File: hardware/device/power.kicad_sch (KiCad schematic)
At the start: 44 parts, among them IC3 SP3401-02UTG, J1 POT_CONN, J2 USB, U20 TPS62A02DRL, U21 TPS560200, U22 MAX17261xxTD, U23 BQ21040DBV, U26 FUSB303BTMX, U27 FUSB302B01MPX, U31 FUSB302B01MPX, U32 LTC2942

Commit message: chore: schematic organization
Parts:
- removed U22: MAX17261xxTD, Package_DFN_QFN:TDFN-14-1EP_3x3mm_P0.4mm_EP1.78x2.35mm, symbol Battery_Management:MAX17261xxTD
- removed U26: FUSB303BTMX, Package_DFN_QFN:Texas_X2QFN-12_1.6x1.6mm_P0.4mm, symbol Interface_USB:FUSB303BTMX
- removed U27: FUSB302B01MPX, Package_DFN_QFN:WQFN-14-1EP_2.5x2.5mm_P0.5mm_EP1.45x1.45mm, symbol Interface_USB:FUSB302B01MPX
- added C19, C20: 1uF, symbol Device:C
- added R38: 675R, Resistor_SMD:R_0402_1005Metric, symbol Device:R
- added U22: BQ24072RGT, Package_DFN_QFN:VQFN-16-1EP_3x3mm_P0.5mm_EP1.6x1.6mm, symbol Battery_Management:BQ24072RGT
- added U26: BQ25040, Package_SON:WSON-10-1EP_2x3mm_P0.5mm_EP0.84x2.4mm_ThermalVias, symbol Battery_Management:BQ25040
- C11, C12, C13, C14, C15, C16, C17, C18, C9, R12, R2, R20, R21, R23, R24, R26, R27, R29, R33: footprint (none) -> Capacitor_SMD:C_0402_1005Metric
- IC3: JLC (none) -> C3702190
- J1: JLC (none) -> C5527934
- J2: JLC (none) -> C2988369
- R34: footprint (none) -> Resistor_SMD:R_0402_1005Metric
- R63, R72: footprint Resistor_SMD:R_0603_1608Metric_Pad0.98x0.95mm_HandSolder -> Capacitor_SMD:C_0402_1005Metric
- U31: JLC (none) -> C488155
- U32: JLC (none) -> C683656
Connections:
- net +3.3V: now also R34.1
- net GND: now also U23.5 (GND), C19.2, C20.2
- net +BATT: now reaches R33.1, U32.1 (SENSE+)
- net +BATT: now also U23.2 (OUT), C20.1
- net at U23.6 (VIN): now also C19.1
- new net: U22.10 (OUT), U22.11 (OUT)
- new net: U22.17 (VSS), U22.8 (VSS)
- new net: U22.2 (BAT), U22.3 (BAT)
- new net: U26.11 (VSS), U26.3 (VSS), U26.7 (VSS)
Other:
- note added: "Charging and draw for battery MUST pass through the fuel gauge current-sense resistor to properly detect discharging."
- note added: "DRP (Dual-Role-Port)"
- note added: "FUSB302B has a "dead battery" feature, enabling Rd resistors on CC lines when the FUSB302B is not powered to allow it to attach as a sink device even when it is not powered."
- note added: "See FUSB302 CONTROL2 register for dual-model device via the autonomous DRP toggle."
- note added: "TODO: checl ISET resistor"
- note added: "Used by the STM32 to detect when a USB cable has been plugged in or removed. Expected signal < 4v"
- note added: "https://www.usb.org/document-library/usb-power-delivery"
- note removed: "BQ24070RHLR?"
- moved on the sheet: BT1, C17, C18, IC3, J2, R29, R33, R34, U23, U31, U32

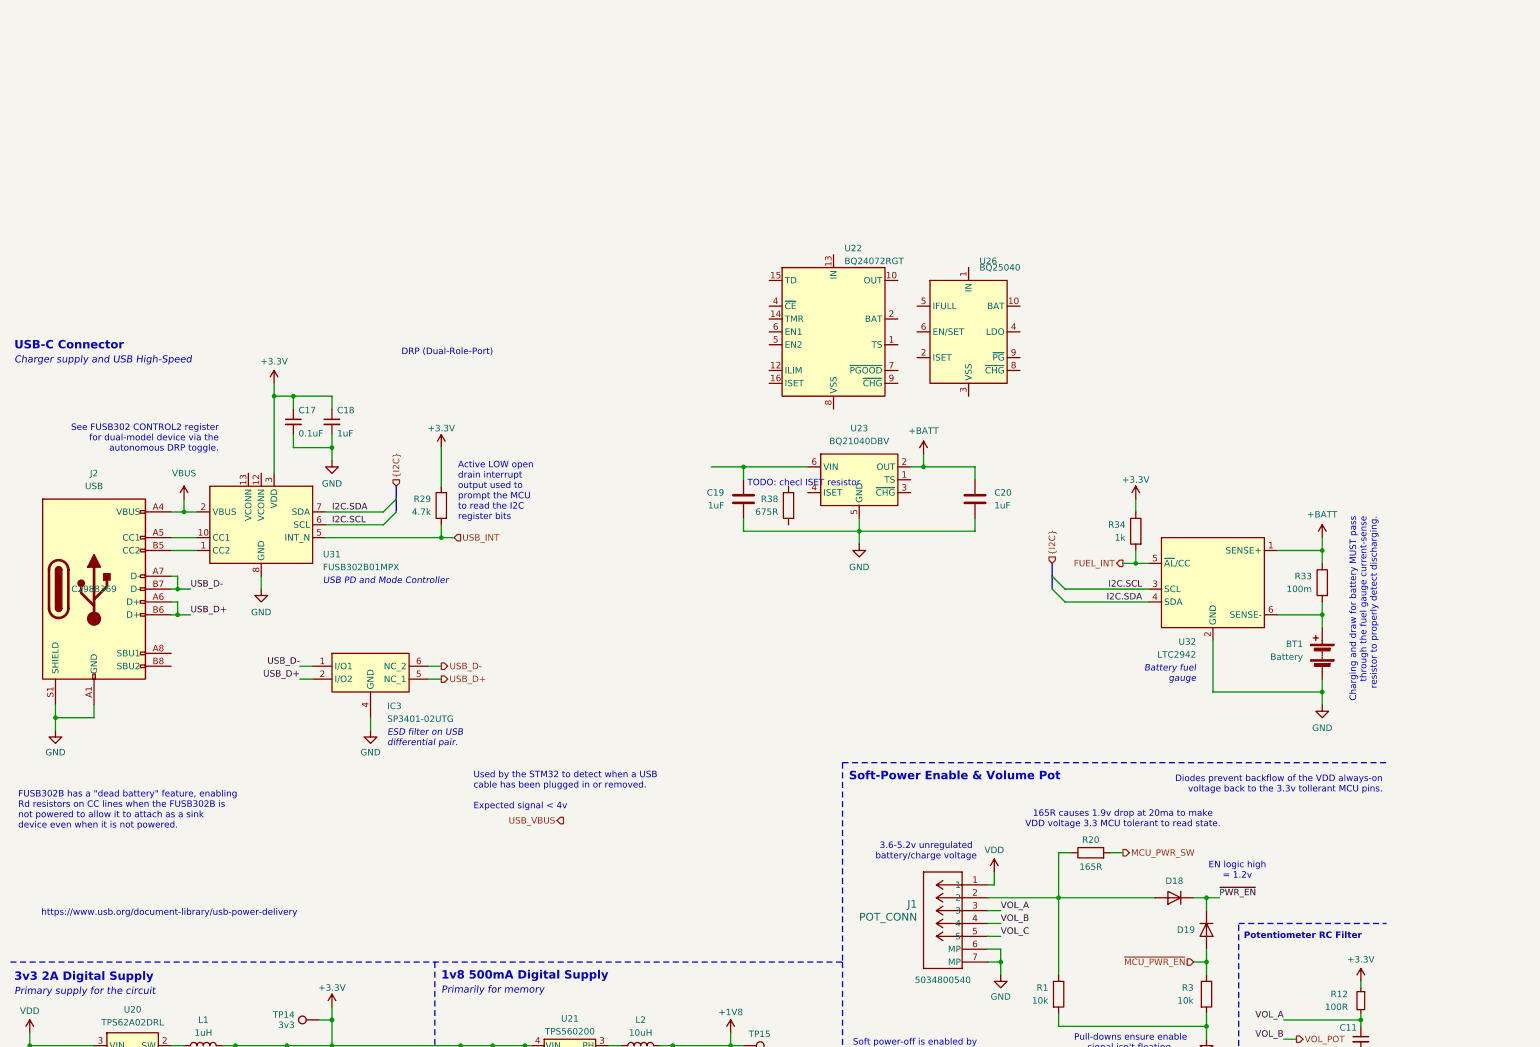
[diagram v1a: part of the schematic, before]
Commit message: feat: add plated mounting holes
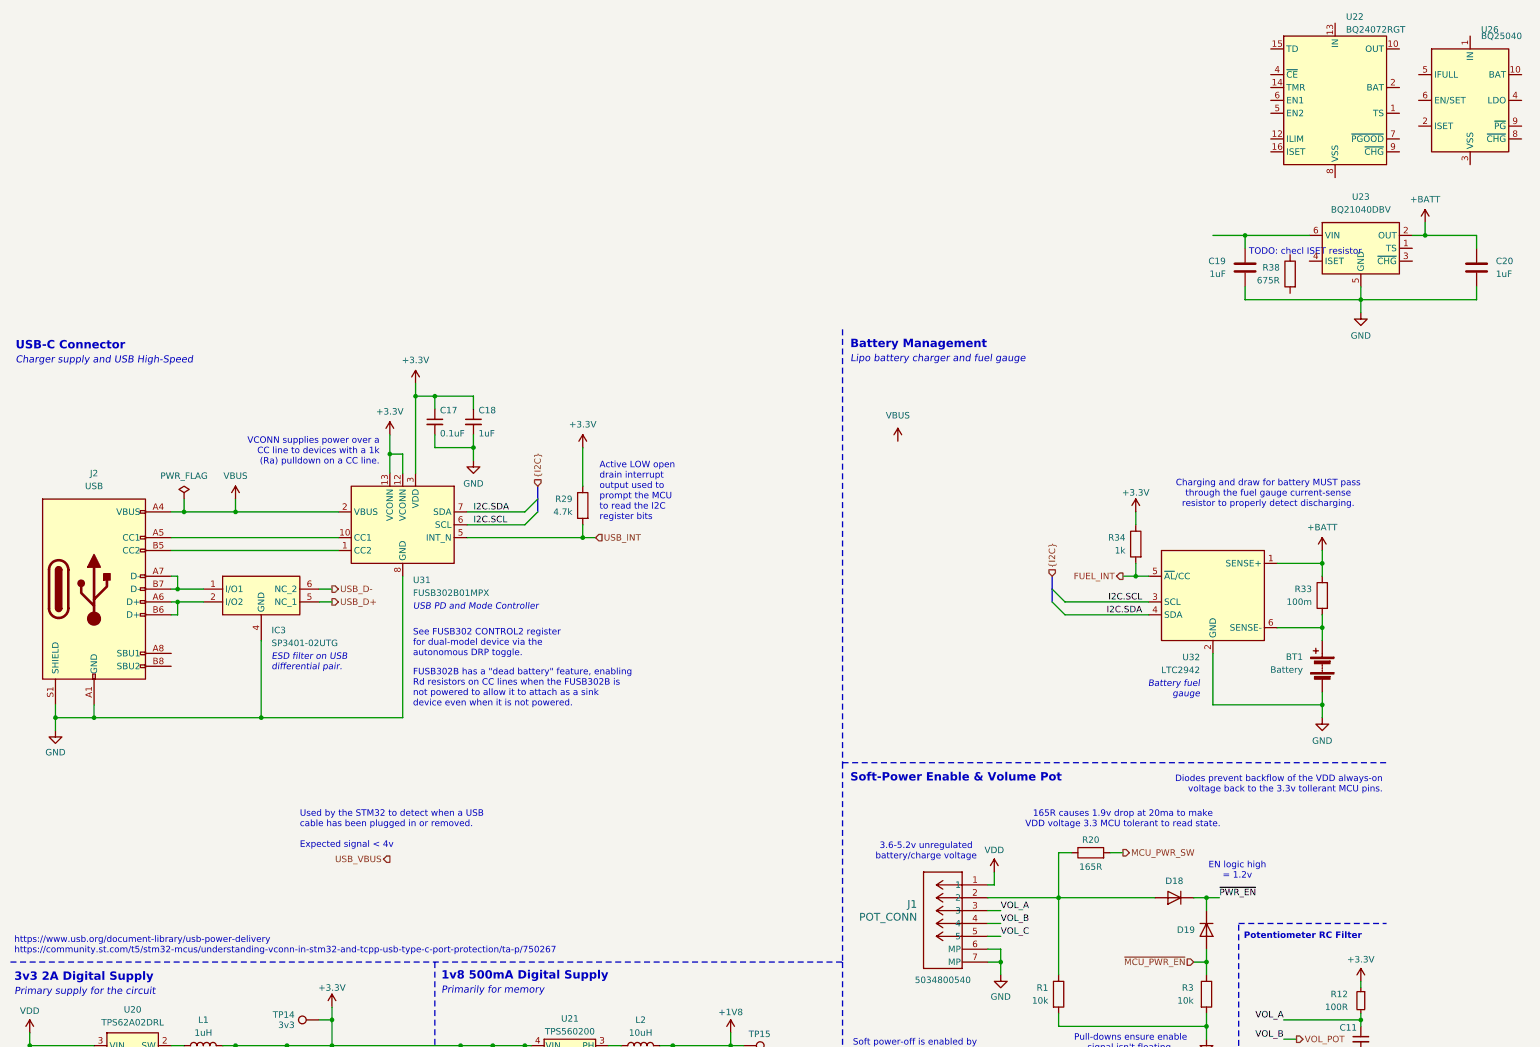
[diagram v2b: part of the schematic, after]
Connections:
- net +3.3V: now also U31.12 (VCONN), U31.13 (VCONN)
- net USB_D+: no longer IC3.2 (I/O2), J2.A6 (D+), J2.B6 (D+)
- net USB_D-: no longer IC3.1 (I/O1), J2.A7 (D-), J2.B7 (D-)
- new net: IC3.2 (I/O2), J2.A6 (D+), J2.B6 (D+)
- new net: IC3.1 (I/O1), J2.A7 (D-), J2.B7 (D-)
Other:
- note added: "Battery Management"
- note added: "Lipo battery charger and fuel gauge"
- note added: "VCONN supplies power over a CC line to devices with a 1k (Ra) pulldown on a CC line."
- note added: "https://www.usb.org/document-library/usb-power-delivery https://community.st.com/t5/stm32-mcus/understanding-vconn-in-stm32-and-tcpp-usb-type-c-port-protection/ta-p/750267"
- note removed: "DRP (Dual-Role-Port)"
- note removed: "https://www.usb.org/document-library/usb-power-delivery"
- moved on the sheet: BT1, C17, C18, C19, C20, IC3, R29, R33, R34, R38, U22, U23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

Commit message: feat: audio system routing
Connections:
- net USB_D+: now also IC3.2 (I/O2), J2.A6 (D+), J2.B6 (D+)
- net USB_D-: now also IC3.1 (I/O1), J2.A7 (D-), J2.B7 (D-)
- net at J2.B5 (CC2), U31.1 (CC2): now also U31.14 (CC2)
- net at J2.A5 (CC1), U31.10 (CC1): now also U31.11 (CC1); no longer U31.14 (CC2)
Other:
- moved on the sheet: IC3
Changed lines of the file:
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@@
 	(text "ESD filter on USB\ndifferential pair."
 		(exclude_from_sim no)
-		(at 64.262 76.2 0)
+		(at 66.802 76.2 0)
 		(effects
 			(font
@@
 	)
 	(junction
-		(at 62.23 88.9)
-		(diameter 0)
-		(color 0 0 0 0)
-	)
-	(junction
 		(at 76.2 153.67)
 		(diameter 0)
@@
 	)
 	(junction
+		(at 64.77 88.9)
+		(diameter 0)
+		(color 0 0 0 0)
+	)
+	(junction
 		(at 57.15 48.26)
 		(diameter 0)
@@
 	(wire
 		(pts
-			(xy 62.23 73.66) (xy 62.23 88.9)
+			(xy 64.77 73.66) (xy 64.77 88.9)
 		)
 		(stroke
@@
 	(wire
 		(pts
-			(xy 29.21 88.9) (xy 62.23 88.9)
+			(xy 29.21 88.9) (xy 64.77 88.9)
 		)
 		(stroke
@@
 		)
 	)
+	(wire
+		(pts
+			(xy 64.77 88.9) (xy 90.17 88.9)
+		)
+		(stroke
+			(width 0)
+			(type default)
+		)
+	)
 	(bus
 		(pts
@@
 	(wire
 		(pts
+			(xy 46.99 50.8) (xy 46.99 53.34)
+		)
+		(stroke
+			(width 0)
+			(type default)
+		)
+	)
+	(wire
+		(pts
 			(xy 132.08 158.75) (xy 130.81 158.75)
 		)
@@
 	(wire
 		(pts
-			(xy 73.66 63.5) (xy 76.2 63.5)
+			(xy 76.2 63.5) (xy 78.74 63.5)
 		)
 		(stroke
@@
 	(wire
 		(pts
-			(xy 62.23 88.9) (xy 90.17 88.9)
-		)
-		(stroke
-			(width 0)
-			(type default)
-		)
-	)
-	(wire
-		(pts
 			(xy 101.6 153.67) (xy 101.6 157.48)
 		)
@@
 	(wire
 		(pts
-			(xy 279.4 147.32) (xy 279.4 148.59)
+			(xy 49.53 53.34) (xy 77.47 53.34)
 		)
 		(stroke
@@
 	(wire
 		(pts
-			(xy 90.17 172.72) (xy 90.17 175.26)
+			(xy 279.4 147.32) (xy 279.4 148.59)
 		)
 		(stroke
@@
 	(wire
 		(pts
-			(xy 132.08 166.37) (xy 132.08 158.75)
+			(xy 90.17 172.72) (xy 90.17 175.26)
 		)
 		(stroke
@@
 	(wire
 		(pts
-			(xy 107.95 167.64) (xy 107.95 179.07)
+			(xy 132.08 166.37) (xy 132.08 158.75)
 		)
 		(stroke
@@
 	(wire
 		(pts
-			(xy 246.38 137.16) (xy 248.92 137.16)
+			(xy 107.95 167.64) (xy 107.95 179.07)
 		)
 		(stroke
@@
 	(wire
 		(pts
-			(xy 279.4 140.97) (xy 279.4 142.24)
+			(xy 246.38 137.16) (xy 248.92 137.16)
 		)
 		(stroke
@@
 	(wire
 		(pts
-			(xy 264.16 148.59) (xy 279.4 148.59)
+			(xy 279.4 140.97) (xy 279.4 142.24)
 		)
 		(stroke
@@
 	(wire
 		(pts
-			(xy 44.45 55.88) (xy 77.47 55.88)
+			(xy 264.16 148.59) (xy 279.4 148.59)
 		)
 		(stroke
@@
 	(wire
 		(pts
+			(xy 77.47 50.8) (xy 46.99 50.8)
+		)
+		(stroke
+			(width 0)
+			(type default)
+		)
+	)
+	(wire
+		(pts
 			(xy 271.78 88.9) (xy 271.78 86.36)
 		)
@@
 	(wire
 		(pts
+			(xy 44.45 55.88) (xy 49.53 55.88)
+		)
+		(stroke
+			(width 0)
+			(type default)
+		)
+	)
+	(wire
+		(pts
 			(xy 237.49 68.58) (xy 220.98 68.58)
 		)
@@
 	(wire
 		(pts
-			(xy 73.66 66.04) (xy 76.2 66.04)
+			(xy 76.2 66.04) (xy 78.74 66.04)
 		)
 		(stroke
@@
 	(wire
 		(pts
+			(xy 49.53 55.88) (xy 49.53 53.34)
+		)
+		(stroke
+			(width 0)
+			(type default)
+		)
+	)
+	(wire
+		(pts
 			(xy 271.78 68.58) (xy 271.78 71.12)
 		)
@@
 	(wire
 		(pts
-			(xy 50.8 63.5) (xy 45.72 63.5)
+			(xy 53.34 63.5) (xy 45.72 63.5)
 		)
 		(stroke
@@
 	(wire
 		(pts
-			(xy 44.45 53.34) (xy 77.47 53.34)
-		)
-		(stroke
-			(width 0)
-			(type default)
-		)
-	)
-	(wire
-		(pts
 			(xy 27.94 156.21) (xy 29.21 156.21)
 		)
@@
 	(wire
 		(pts
+			(xy 46.99 53.34) (xy 44.45 53.34)
+		)
+		(stroke
+			(width 0)
+			(type default)
+		)
+	)
+	(wire
+		(pts
 			(xy 57.15 153.67) (xy 67.31 153.67)
 		)
@@
 	(wire
 		(pts
-			(xy 50.8 66.04) (xy 45.72 66.04)
+			(xy 53.34 66.04) (xy 45.72 66.04)
 		)
 		(stroke
@@
 		)
 	)
+	(label "USB_D-"
+		(at 46.99 63.5 0)
+		(effects
+			(font
+				(size 1.27 1.27)
+			)
+			(justify left bottom)
+		)
+	)
 	(label "I2C.SDA"
 		(at 104.14 48.26 0)
@@
 		)
 	)
+	(label "USB_D+"
+		(at 46.99 66.04 0)
+		(effects
+			(font
+				(size 1.27 1.27)
+			)
+			(justify left bottom)
+		)
+	)
 	(label "I2C.SDA"
 		(at 236.22 68.58 180)
@@
 	(hierarchical_label "USB_D+"
 		(shape output)
-		(at 76.2 66.04 0)
+		(at 78.74 66.04 0)
 		(effects
 			(font
@@
 	(hierarchical_label "USB_D-"
 		(shape output)
-		(at 76.2 63.5 0)
+		(at 78.74 63.5 0)
 		(effects
 			(font
@@
 	)
 	(symbol
-		(lib_name "FUSB302B01MPX_1")
 		(lib_id "Interface_USB:FUSB302B01MPX")
 		(at 90.17 50.8 0)
@@
 	(symbol
 		(lib_id "pocket_synth:SP3401-02UTG")
-		(at 62.23 64.77 0)
+		(at 64.77 64.77 0)
 		(unit 1)
 		(exclude_from_sim no)
@@
 		(dnp no)
 		(property "Reference" "IC3"
-			(at 64.262 71.628 0)
+			(at 66.802 71.628 0)
 			(effects
 				(font
@@
 		)
 		(property "Value" "SP3401-02UTG"
-			(at 64.262 74.168 0)
+			(at 66.802 74.168 0)
 			(effects
 				(font
@@
 		)
 		(property "Footprint" "pocket_synth:SP340102UTG"
-			(at 88.9 159.69 0)
+			(at 91.44 159.69 0)
 			(effects
 				(font
@@
 		)
 		(property "Datasheet" "https://m.littelfuse.com/~/media/electronics/datasheets/tvs_diode_arrays/littelfuse_tvs_diode_array_sp3401_datasheet.pdf.pdf"
-			(at 88.9 259.69 0)
+			(at 91.44 259.69 0)
 			(effects
 				(font
@@
 		)
 		(property "Description" "ESD Suppressors / TVS Diodes 28KV 0.6pF 3.3V 10A uDFN-6 TVS Array"
-			(at 62.23 64.77 0)
+			(at 64.77 64.77 0)
 			(effects
 				(font
@@
 		)
 		(property "Height" "0.55"
-			(at 88.9 459.69 0)
+			(at 91.44 459.69 0)
 			(effects
 				(font
@@
 		)
 		(property "Mouser Part Number" "576-SP3401-02UTG"
-			(at 88.9 559.69 0)
+			(at 91.44 559.69 0)
 			(effects
 				(font
@@
 		)
 		(property "Mouser Price/Stock" "https://www.mouser.co.uk/ProductDetail/Littelfuse/SP3401-02UTG?qs=T3oQrply3y%2FjRDLmSQJ5ww%3D%3D"
-			(at 88.9 659.69 0)
+			(at 91.44 659.69 0)
 			(effects
 				(font
@@
 		)
 		(property "Manufacturer_Name" "LITTELFUSE"
-			(at 88.9 759.69 0)
+			(at 91.44 759.69 0)
 			(effects
 				(font
@@
 		)
 		(property "Manufacturer_Part_Number" "SP3401-02UTG"
-			(at 88.9 859.69 0)
+			(at 91.44 859.69 0)
 			(effects
 				(font
@@
 		)
 		(property "JLC" "C3702190"
-			(at 62.23 64.77 0)
+			(at 64.77 64.77 0)
 			(effects
 				(font
